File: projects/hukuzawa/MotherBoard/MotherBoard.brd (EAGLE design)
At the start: 78.7 x 53.3 mm, 27 parts, among them IC1 PIC16F886, Q1 CERALOCK

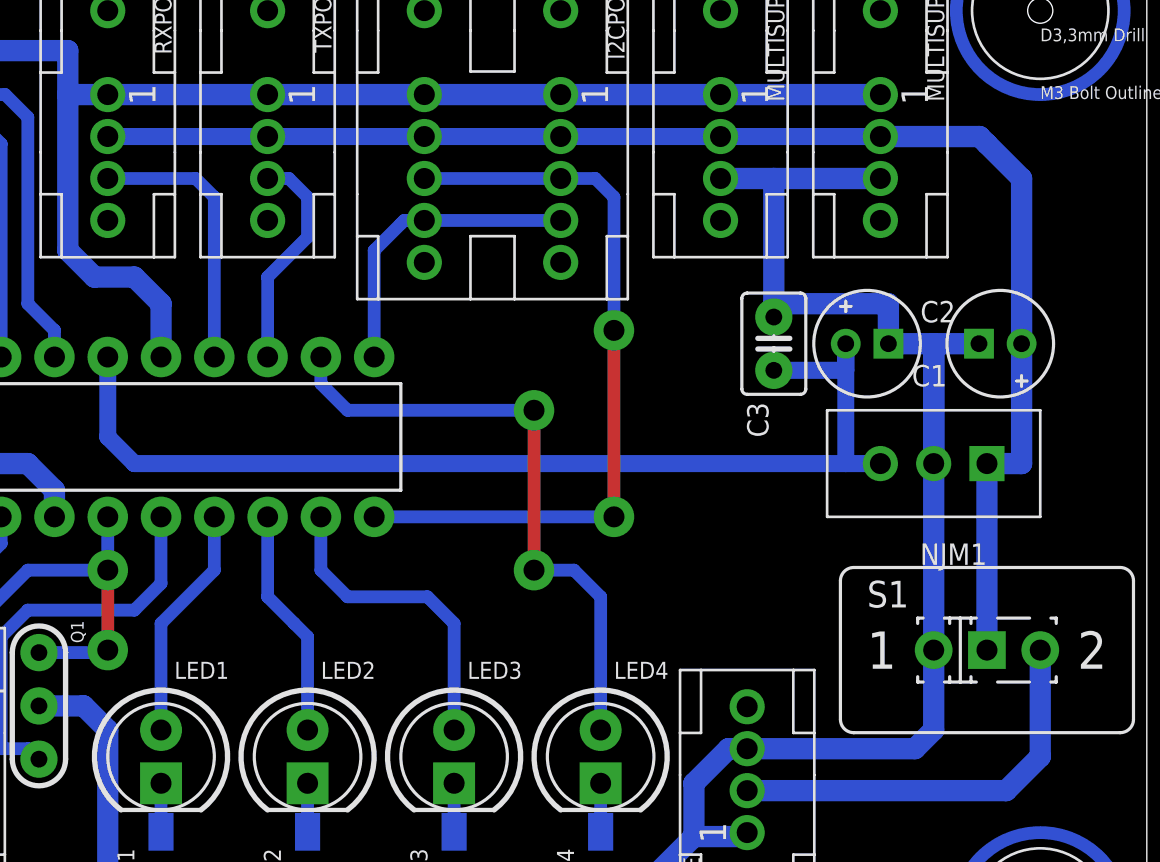
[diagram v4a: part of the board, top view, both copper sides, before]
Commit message: マザーボード回路 v1.21
PICから外部に流す電源を制御するよう仕様変更
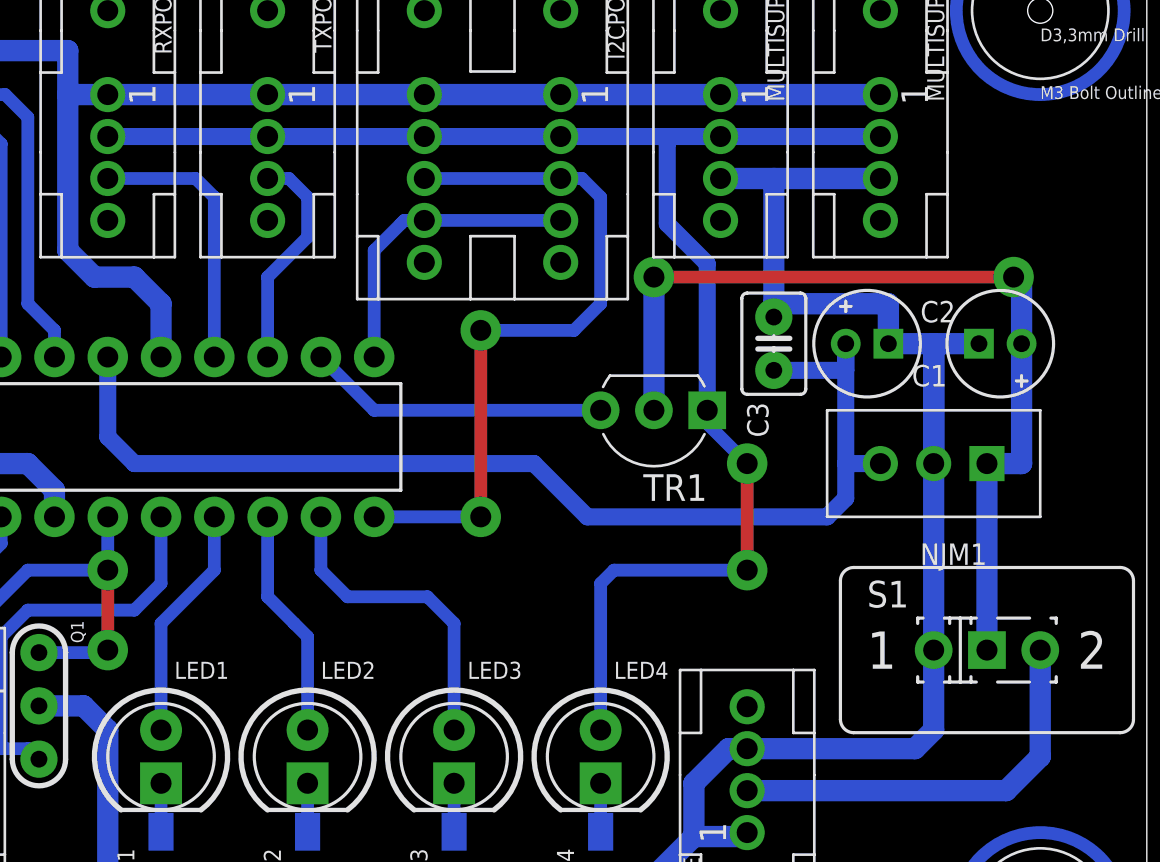
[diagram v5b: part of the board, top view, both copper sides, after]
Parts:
- added TR1: 2SC1815, FP-21T for MITS:TO92-
- R4: value 1k -> 10k
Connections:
- removed net OPRLED: IC1.16, LED4.A
- new net CTRLSUPP: I2CPORT.1-2, I2CPORT.2-2, LED4.A, MULTISUPPA.1-2, MULTISUPPB.1-2, RXPORT.1-2, TR1.E, TXPORT.1-2
- new net OPR: IC1.16, TR1.B
- net V+: now also TR1.C; no longer I2CPORT.1-2, I2CPORT.2-2, MULTISUPPA.1-2, MULTISUPPB.1-2, RXPORT.1-2, TXPORT.1-2
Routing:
- net CTRLSUPP: track 0.00 -> 73.7 mm, vias 0 -> 2
- net OPRLED: track 29.6 -> 0.00 mm, vias 2 -> 0
- net V+: track 68.5 -> 43.3 mm, vias 0 -> 2
- net OPR: track 0.00 -> 14.4 mm
- net +5V: track 51.6 -> 54.7 mm
- net SCL: track 36.1 -> 34.1 mm
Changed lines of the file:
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@@
 <attribute name="VALUE" x="47.625" y="6.985" size="0.8128" layer="27" rot="R90"/>
 </element>
-<element name="R4" library="rcl" package="R3216W" value="1k" x="52.705" y="7.62" smashed="yes" rot="MR270">
+<element name="R4" library="rcl" package="R3216W" value="10k" x="52.705" y="7.62" smashed="yes" rot="MR270">
 <attribute name="NAME" x="51.435" y="6.985" size="0.8128" layer="25" rot="R90"/>
 <attribute name="VALUE" x="54.61" y="6.985" size="0.8128" layer="27" rot="R90"/>
@@
 <element name="HOLE2" library="Hole" package="HOLE3.3" value="HOLE3.3M3BOLT" x="5.08" y="48.26"/>
 <element name="HOLE1" library="Hole" package="HOLE3.3" value="HOLE3.3M3BOLT" x="5.08" y="5.08"/>
+<element name="TR1" library="FP-21T for MITS" package="TO92-" value="2SC1815" x="55.245" y="29.21" rot="R180"/>
 </elements>
 <signals>
@@
 <contactref element="I2CPORT" pad="2-3"/>
 <wire x1="44.3" y1="40.26" x2="50.8" y2="40.26" width="0.6096" layer="16"/>
-<wire x1="41.91" y1="24.13" x2="53.34" y2="24.13" width="0.6096" layer="16"/>
-<wire x1="50.8" y1="40.26" x2="52.45" y2="40.26" width="0.6096" layer="16"/>
-<wire x1="52.45" y1="40.26" x2="53.34" y2="39.37" width="0.6096" layer="16"/>
-<via x="53.34" y="24.13" extent="1-16" drill="1" diameter="1.9304"/>
-<wire x1="53.34" y1="24.13" x2="53.34" y2="33.02" width="0.6096" layer="1"/>
-<via x="53.34" y="33.02" extent="1-16" drill="1" diameter="1.9304"/>
-<wire x1="53.34" y1="33.02" x2="53.34" y2="39.37" width="0.6096" layer="16"/>
+<wire x1="41.91" y1="24.13" x2="46.99" y2="24.13" width="0.6096" layer="16"/>
+<wire x1="50.8" y1="40.26" x2="51.815" y2="40.26" width="0.6096" layer="16"/>
+<wire x1="51.815" y1="40.26" x2="52.705" y2="39.37" width="0.6096" layer="16"/>
+<via x="46.99" y="24.13" extent="1-16" drill="1" diameter="1.9304"/>
+<wire x1="46.99" y1="24.13" x2="46.99" y2="33.02" width="0.6096" layer="1"/>
+<via x="46.99" y="33.02" extent="1-16" drill="1" diameter="1.9304"/>
+<wire x1="52.705" y1="39.37" x2="52.705" y2="34.29" width="0.6096" layer="16"/>
+<wire x1="52.705" y1="34.29" x2="51.435" y2="33.02" width="0.6096" layer="16"/>
+<wire x1="51.435" y1="33.02" x2="46.99" y2="33.02" width="0.6096" layer="16"/>
 </signal>
 <signal name="SDA">
@@
 <contactref element="C1" pad="+"/>
 <contactref element="S1" pad="2"/>
-<contactref element="RXPORT" pad="1-2"/>
-<contactref element="TXPORT" pad="1-2"/>
-<contactref element="I2CPORT" pad="1-2"/>
-<contactref element="I2CPORT" pad="2-2"/>
-<contactref element="MULTISUPPA" pad="1-2"/>
-<contactref element="MULTISUPPB" pad="1-2"/>
-<wire x1="29.21" y1="42.26" x2="36.83" y2="42.26" width="0.8128" layer="16"/>
-<wire x1="36.83" y1="42.26" x2="44.3" y2="42.26" width="0.8128" layer="16"/>
-<wire x1="44.3" y1="42.26" x2="50.8" y2="42.26" width="0.8128" layer="16"/>
-<wire x1="50.8" y1="42.26" x2="58.42" y2="42.26" width="0.8128" layer="16"/>
-<wire x1="58.42" y1="42.26" x2="66.04" y2="42.26" width="0.8128" layer="16"/>
 <wire x1="71.12" y1="17.78" x2="71.12" y2="26.67" width="1.016" layer="16"/>
+<wire x1="72.771" y1="26.67" x2="72.771" y2="32.385" width="1.016" layer="16"/>
+<contactref element="TR1" pad="C"/>
 <wire x1="71.12" y1="26.67" x2="72.771" y2="26.67" width="1.016" layer="16"/>
-<wire x1="72.771" y1="26.67" x2="72.771" y2="32.385" width="1.016" layer="16"/>
-<wire x1="66.04" y1="42.26" x2="70.77" y2="42.26" width="1.016" layer="16"/>
-<wire x1="70.77" y1="42.26" x2="71.12" y2="41.91" width="1.016" layer="16"/>
-<wire x1="72.771" y1="32.385" x2="72.771" y2="40.259" width="1.016" layer="16"/>
-<wire x1="72.771" y1="40.259" x2="71.12" y2="41.91" width="1.016" layer="16"/>
+<wire x1="72.771" y1="32.385" x2="72.771" y2="35.56" width="1.016" layer="16"/>
+<wire x1="72.771" y1="35.56" x2="72.39" y2="35.56" width="1.016" layer="16"/>
+<via x="72.39" y="35.56" extent="1-16" drill="1" diameter="1.9304"/>
+<wire x1="72.39" y1="35.56" x2="55.245" y2="35.56" width="0.6096" layer="1"/>
+<via x="55.245" y="35.56" extent="1-16" drill="1" diameter="1.9304"/>
+<wire x1="55.245" y1="35.56" x2="55.245" y2="29.21" width="1.016" layer="16"/>
 </signal>
 <signal name="GND">
@@
 <wire x1="29.21" y1="31.75" x2="29.21" y2="27.94" width="0.8128" layer="16"/>
 <wire x1="29.21" y1="27.94" x2="30.48" y2="26.67" width="0.8128" layer="16"/>
-<wire x1="30.48" y1="26.67" x2="63.5" y2="26.67" width="0.8128" layer="16"/>
-<wire x1="64.389" y1="26.67" x2="63.5" y2="26.67" width="0.8128" layer="16"/>
+<wire x1="30.48" y1="26.67" x2="49.53" y2="26.67" width="0.8128" layer="16"/>
+<wire x1="49.53" y1="26.67" x2="52.07" y2="24.13" width="0.8128" layer="16"/>
+<wire x1="64.389" y1="26.67" x2="64.389" y2="25.019" width="0.8128" layer="16"/>
+<wire x1="64.389" y1="25.019" x2="63.5" y2="24.13" width="0.8128" layer="16"/>
+<wire x1="63.5" y1="24.13" x2="52.07" y2="24.13" width="0.8128" layer="16"/>
 </signal>
 <signal name="N$6">
@@
 <wire x1="45.72" y1="19.05" x2="45.72" y2="13.97" width="0.6096" layer="16"/>
 </signal>
-<signal name="OPRLED">
-<contactref element="LED4" pad="A"/>
+<signal name="OPR">
 <contactref element="IC1" pad="16"/>
-<wire x1="39.37" y1="31.75" x2="39.37" y2="30.48" width="0.6096" layer="16"/>
-<wire x1="39.37" y1="30.48" x2="40.64" y2="29.21" width="0.6096" layer="16"/>
-<wire x1="40.64" y1="29.21" x2="49.53" y2="29.21" width="0.6096" layer="16"/>
-<via x="49.53" y="29.21" extent="1-16" drill="1" diameter="1.9304"/>
-<wire x1="49.53" y1="29.21" x2="49.53" y2="21.59" width="0.6096" layer="1"/>
-<via x="49.53" y="21.59" extent="1-16" drill="1" diameter="1.9304"/>
-<wire x1="49.53" y1="21.59" x2="51.435" y2="21.59" width="0.6096" layer="16"/>
-<wire x1="51.435" y1="21.59" x2="52.705" y2="20.32" width="0.6096" layer="16"/>
-<wire x1="52.705" y1="20.32" x2="52.705" y2="13.97" width="0.6096" layer="16"/>
+<contactref element="TR1" pad="B"/>
+<wire x1="39.37" y1="31.75" x2="41.91" y2="29.21" width="0.6096" layer="16"/>
+<wire x1="41.91" y1="29.21" x2="52.705" y2="29.21" width="0.6096" layer="16"/>
 </signal>
 <signal name="B7">
@@
 <wire x1="45.72" y1="11.43" x2="45.72" y2="9.119" width="0.6096" layer="16"/>
 </signal>
+<signal name="CTRLSUPP">
+<contactref element="TR1" pad="E"/>
+<contactref element="RXPORT" pad="1-2"/>
+<contactref element="TXPORT" pad="1-2"/>
+<contactref element="I2CPORT" pad="1-2"/>
+<contactref element="I2CPORT" pad="2-2"/>
+<wire x1="44.3" y1="42.26" x2="50.8" y2="42.26" width="0.8128" layer="16"/>
+<contactref element="MULTISUPPA" pad="1-2"/>
+<contactref element="MULTISUPPB" pad="1-2"/>
+<wire x1="58.42" y1="42.26" x2="66.04" y2="42.26" width="0.8128" layer="16"/>
+<wire x1="57.785" y1="29.21" x2="57.785" y2="36.195" width="0.8128" layer="16"/>
+<wire x1="57.785" y1="36.195" x2="55.88" y2="38.1" width="0.8128" layer="16"/>
+<wire x1="29.21" y1="42.26" x2="36.83" y2="42.26" width="0.8128" layer="16"/>
+<wire x1="36.83" y1="42.26" x2="44.3" y2="42.26" width="0.8128" layer="16"/>
+<wire x1="58.42" y1="42.26" x2="55.88" y2="42.26" width="0.8128" layer="16"/>
+<wire x1="55.88" y1="42.26" x2="55.88" y2="41.91" width="0.8128" layer="16"/>
+<wire x1="55.88" y1="41.91" x2="55.88" y2="38.1" width="0.8128" layer="16"/>
+<wire x1="50.8" y1="42.26" x2="55.88" y2="42.26" width="0.8128" layer="16"/>
+<wire x1="55.88" y1="42.26" x2="55.88" y2="41.91" width="0.8128" layer="16"/>
+<contactref element="LED4" pad="A"/>
+<wire x1="57.785" y1="29.21" x2="57.785" y2="28.575" width="0.6096" layer="16"/>
+<wire x1="57.785" y1="28.575" x2="59.69" y2="26.67" width="0.6096" layer="16"/>
+<via x="59.69" y="26.67" extent="1-16" drill="1" diameter="1.9304"/>
+<wire x1="52.705" y1="13.97" x2="52.705" y2="20.955" width="0.6096" layer="16"/>
+<wire x1="52.705" y1="20.955" x2="53.34" y2="21.59" width="0.6096" layer="16"/>
+<wire x1="53.34" y1="21.59" x2="59.69" y2="21.59" width="0.6096" layer="16"/>
+<via x="59.69" y="21.59" extent="1-16" drill="1" diameter="1.9304"/>
+<wire x1="59.69" y1="21.59" x2="59.69" y2="26.67" width="0.6096" layer="1"/>
+</signal>
 </signals>

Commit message: マザーボード修正
規格化されたポートを分離、ライブラリを新規に作成
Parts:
- BATTLINE, MULTISUPPA, MULTISUPPB: value 3X1A -> POWERPORT; device 3M_372xx:37203-62A3-003 -> 3M_Ports:37203-62A3-003
- I2CPORT: value 4X2 -> I2CPORTX2; device 3M_372xx:37208-62A3-004 -> 3M_Ports:37208-62A3-004
- RXPORT: value 3X1A -> RS232RXPORT; device 3M_372xx:37203-62A3-003 -> 3M_Ports:37203-62A3-003
- TXPORT: value 3X1A -> RS232TXPORT; device 3M_372xx:37203-62A3-003 -> 3M_Ports:37203-62A3-003
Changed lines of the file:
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@@
 </autorouter>
 <elements>
-<element name="BATTLINE" library="3M_372xx" package="37203-62A3-003" value="3X1A" x="59.69" y="5.08" smashed="yes">
+<element name="BATTLINE" library="3M_Ports" package="37203-62A3-003" value="POWERPORT" x="59.69" y="5.08" smashed="yes">
 <attribute name="NAME" x="57.46" y="3.08" size="0.8128" layer="25" rot="R90"/>
 <attribute name="VALUE" x="62.92" y="3.08" size="0.8128" layer="27" rot="R90"/>
@@
 <attribute name="VALUE" x="54.61" y="6.985" size="0.8128" layer="27" rot="R90"/>
 </element>
-<element name="TXPORT" library="3M_372xx" package="37203-62A3-003" value="3X1A" x="36.83" y="48.26" smashed="yes" rot="R180">
+<element name="TXPORT" library="3M_Ports" package="37203-62A3-003" value="RS232TXPORT" x="36.83" y="48.26" smashed="yes" rot="R180">
 <attribute name="NAME" x="39.06" y="50.26" size="0.8128" layer="25" rot="R270"/>
 <attribute name="VALUE" x="33.6" y="50.26" size="0.8128" layer="27" rot="R270"/>
 </element>
-<element name="RXPORT" library="3M_372xx" package="37203-62A3-003" value="3X1A" x="29.21" y="48.26" smashed="yes" rot="R180">
+<element name="RXPORT" library="3M_Ports" package="37203-62A3-003" value="RS232RXPORT" x="29.21" y="48.26" smashed="yes" rot="R180">
 <attribute name="NAME" x="31.44" y="50.26" size="0.8128" layer="25" rot="R270"/>
 <attribute name="VALUE" x="25.98" y="50.26" size="0.8128" layer="27" rot="R270"/>
@@
 <attribute name="VALUE" x="9.955" y="50.26" size="0.8128" layer="27" rot="R270"/>
 </element>
-<element name="I2CPORT" library="3M_372xx" package="37208-62A3-004" value="4X2" x="50.8" y="48.26" smashed="yes" rot="R180">
+<element name="I2CPORT" library="3M_Ports" package="37208-62A3-004" value="I2CPORTX2" x="50.8" y="48.26" smashed="yes" rot="R180">
 <attribute name="NAME" x="53.03" y="50.26" size="0.8128" layer="25" rot="R270"/>
 <attribute name="VALUE" x="41.07" y="50.26" size="0.8128" layer="27" rot="R270"/>
 </element>
 <element name="Q1" library="FP-21T for MITS" package="CERALOCK" value="CERALOCK" x="25.93" y="15.12" rot="R270"/>
-<element name="MULTISUPPB" library="3M_372xx" package="37203-62A3-003" value="3X1A" x="58.42" y="48.26" smashed="yes" rot="R180">
+<element name="MULTISUPPB" library="3M_Ports" package="37203-62A3-003" value="POWERPORT" x="58.42" y="48.26" smashed="yes" rot="R180">
 <attribute name="NAME" x="60.65" y="50.26" size="0.8128" layer="25" rot="R270"/>
 <attribute name="VALUE" x="55.19" y="50.26" size="0.8128" layer="27" rot="R270"/>
 </element>
-<element name="MULTISUPPA" library="3M_372xx" package="37203-62A3-003" value="3X1A" x="66.04" y="48.26" smashed="yes" rot="R180">
+<element name="MULTISUPPA" library="3M_Ports" package="37203-62A3-003" value="POWERPORT" x="66.04" y="48.26" smashed="yes" rot="R180">
 <attribute name="NAME" x="68.27" y="50.26" size="0.8128" layer="25" rot="R270"/>
 <attribute name="VALUE" x="62.81" y="50.26" size="0.8128" layer="27" rot="R270"/>
